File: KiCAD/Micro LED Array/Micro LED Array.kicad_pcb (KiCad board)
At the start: 2 copper layers, 36 parts

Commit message: 56 strip 2
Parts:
- added D37: LED, Custom footprints:LED_APG0603SEC-E-TT_KNB, F.Cu at (36.5, 38.5)
- added D38: LED, Custom footprints:LED_APG0603SEC-E-TT_KNB, F.Cu at (36.5, 38.9)
- added D39: LED, Custom footprints:LED_APG0603SEC-E-TT_KNB, F.Cu at (36.5, 39.4)
- added D40: LED, Custom footprints:LED_APG0603SEC-E-TT_KNB, F.Cu at (36.5, 39.9)
- added D41: LED, Custom footprints:LED_APG0603SEC-E-TT_KNB, F.Cu at (36.5, 43.8)
- added D42: LED, Custom footprints:LED_APG0603SEC-E-TT_KNB, F.Cu at (36.5, 43.3)
- added D43: LED, Custom footprints:LED_APG0603SEC-E-TT_KNB, F.Cu at (36.5, 42.8)
- added D44: LED, Custom footprints:LED_APG0603SEC-E-TT_KNB, F.Cu at (36.5, 42.3)
- added D45: LED, Custom footprints:LED_APG0603SEC-E-TT_KNB, F.Cu at (36.5, 41.9)
- added D46: LED, Custom footprints:LED_APG0603SEC-E-TT_KNB, F.Cu at (36.5, 41.4)
- added D47: LED, Custom footprints:LED_APG0603SEC-E-TT_KNB, F.Cu at (36.5, 40.9)
- added D48: LED, Custom footprints:LED_APG0603SEC-E-TT_KNB, F.Cu at (36.5, 40.4)
- added D49: LED, Custom footprints:LED_APG0603SEC-E-TT_KNB, F.Cu at (36.5, 44.3)
- added D50: LED, Custom footprints:LED_APG0603SEC-E-TT_KNB, F.Cu at (36.5, 44.8)
- added D51: LED, Custom footprints:LED_APG0603SEC-E-TT_KNB, F.Cu at (36.5, 45.2)
- added D52: LED, Custom footprints:LED_APG0603SEC-E-TT_KNB, F.Cu at (36.5, 45.7)
- added D53: LED, Custom footprints:LED_APG0603SEC-E-TT_KNB, F.Cu at (36.5, 46.2)
- added D54: LED, Custom footprints:LED_APG0603SEC-E-TT_KNB, F.Cu at (36.5, 46.7)
- added D55: LED, Custom footprints:LED_APG0603SEC-E-TT_KNB, F.Cu at (36.5, 47.2)
- added D56: LED, Custom footprints:LED_APG0603SEC-E-TT_KNB, F.Cu at (36.5, 47.7)
- D1, D10, D11, D12, D13, D14, D15, D16, D17, D18, D19, D2, D20, D21, D22, D23, D24, D25, D26, D27, D28, D29, D3, D30, D31, D32, D33, D34, D35, D36, D4, D5, D6, D7, D8, D9: footprint Custom footprints:LED_APG0603SEC-E-TT_KNB - with via -> Custom footprints:LED_APG0603SEC-E-TT_KNB
- moved D25 56.8 mm to (36.5, 36.0), turned to 180 degrees
- moved D26 55.4 mm to (36.5, 35.5)
- moved D9 55.1 mm to (36.5, 28.3), turned to 180 degrees
- moved D1 54.9 mm to (36.5, 21.0)
- moved D7 54.5 mm to (36.5, 23.9)
- moved D2 54.5 mm to (36.5, 21.5), turned to 180 degrees
- moved D19 54.3 mm to (36.5, 29.7)
- moved D10 54.1 mm to (36.5, 27.8)
- moved D27 54.1 mm to (36.5, 35.1), turned to 180 degrees
- moved D3 54.1 mm to (36.5, 22.0)
- moved D13 54.0 mm to (36.5, 26.3), turned to 180 degrees
- moved D8 54.0 mm to (36.5, 24.4), turned to 180 degrees
- moved D20 53.7 mm to (36.5, 30.2), turned to 180 degrees
- moved D4 53.7 mm to (36.5, 22.5), turned to 180 degrees
- moved D33 53.6 mm to (36.5, 36.5)
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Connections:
- D11 pad 1: Net-(D11-K) -> Net-(D10-A)
- D11 pad 2: Net-(D10-K) -> Net-(D11-A)
- D12 pad 1: Net-(D12-K) -> Net-(D11-A)
- D12 pad 2: Net-(D11-K) -> Net-(D12-A)
- D13 pad 1: Net-(D13-K) -> Net-(D12-A)
- D13 pad 2: Net-(D12-K) -> Net-(D13-A)
- D14 pad 1: Net-(D14-K) -> Net-(D13-A)
- D14 pad 2: Net-(D13-K) -> Net-(D14-A)
- D15 pad 1: Net-(D15-K) -> Net-(D14-A)
- D15 pad 2: Net-(D14-K) -> Net-(D15-A)
- D16 pad 1: Net-(D16-K) -> Net-(D15-A)
- D16 pad 2: Net-(D15-K) -> Net-(D16-A)
- D17 pad 2: Net-(D16-K) -> Net-(D17-A)
- D25 pad 2: Net-(D24-K) -> Net-(D25-A)
- D26 pad 1: Net-(D26-K) -> Net-(D25-A)
- D26 pad 2: Net-(D25-K) -> Net-(D26-A)
- D27 pad 1: Net-(D27-K) -> Net-(D26-A)
- D27 pad 2: Net-(D26-K) -> Net-(D27-A)
- D28 pad 1: Net-(D28-K) -> Net-(D27-A)
- D28 pad 2: Net-(D27-K) -> Net-(D28-A)
- D29 pad 1: Net-(D29-K) -> Net-(D28-A)
- D29 pad 2: Net-(D28-K) -> Net-(D29-A)
- D30 pad 1: Net-(D30-K) -> Net-(D29-A)
- D30 pad 2: Net-(D29-K) -> Net-(D30-A)
- D31 pad 1: Net-(D31-K) -> Net-(D30-A)
- D31 pad 2: Net-(D30-K) -> Net-(D31-A)
- D32 pad 1: Net-(D32-K) -> Net-(D31-A)
- D32 pad 2: Net-(D31-K) -> Net-(D24-K)
- D33 pad 2: Net-(D32-K) -> Net-(D25-K)
- D36 pad 1: GND -> Net-(D36-K)
- D8 pad 1: Net-(D8-K) -> Net-(D16-A)
- D9 pad 1: Net-(D10-A) -> Net-(D17-A)
- D9 pad 2: Net-(D8-K) -> Net-(D10-K)

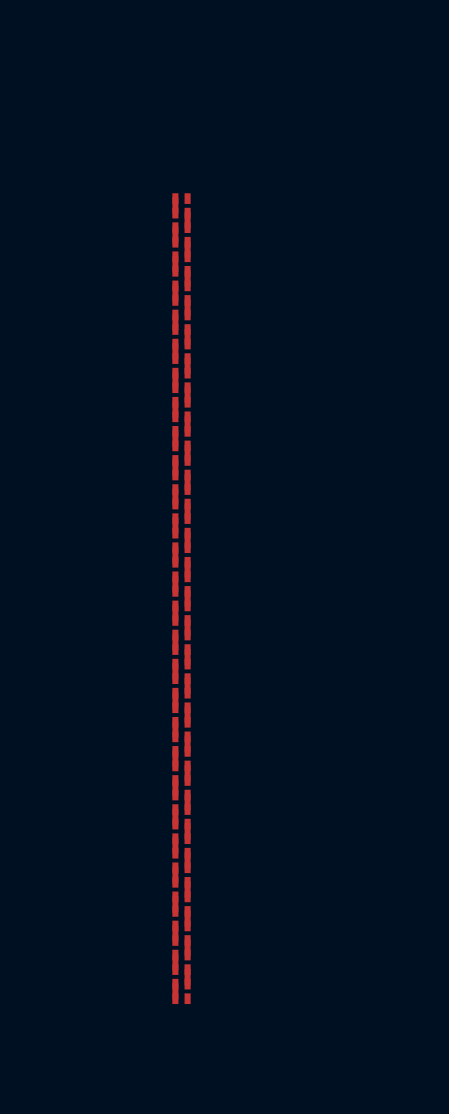
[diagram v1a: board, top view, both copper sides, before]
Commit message: Add bodge pads to diagnose and bypass LEDs
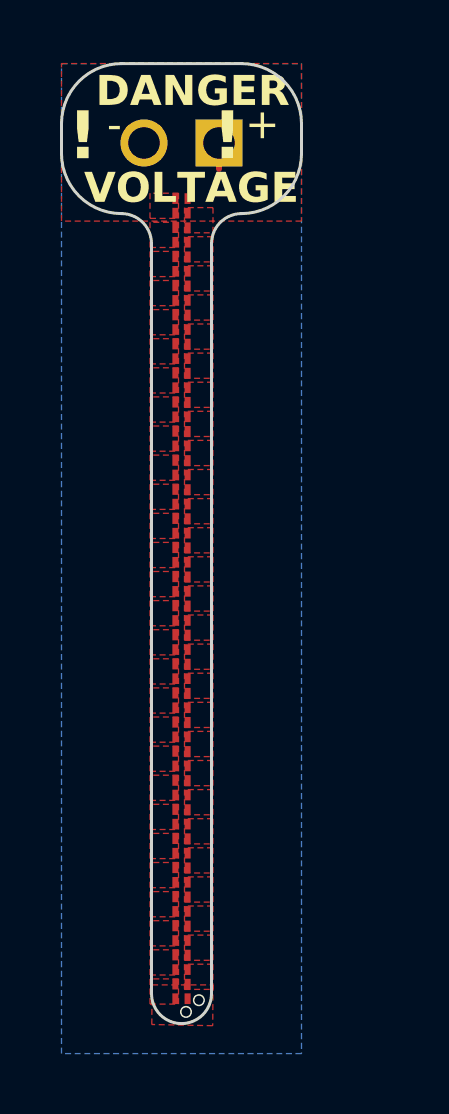
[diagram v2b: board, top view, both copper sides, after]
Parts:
- added J1: JST-XH, Custom footprints:JST_B2B-XH-A, B.Cu at (36.5, 19.7)
- turned D1 to 90 degrees
- turned D10 to 90 degrees
- turned D11 to -90 degrees
- turned D12 to 90 degrees
- turned D13 to -90 degrees
- turned D14 to 90 degrees
- turned D15 to -90 degrees
- turned D16 to 90 degrees
- turned D17 to 90 degrees
- turned D18 to -90 degrees
- turned D19 to 90 degrees
- turned D2 to -90 degrees
- turned D20 to -90 degrees
- turned D21 to 90 degrees
- turned D22 to -90 degrees
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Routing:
- net VDD: track 0.00 -> 0.87 mm
- net GND: vias 0 -> 2
- added copper zone on B.Cu, net GND
- added copper zone on F.Cu, net GND
- added copper zone on F.Cu, net Net-(D1-K)
- added copper zone on F.Cu, net Net-(D10-A)
- added copper zone on F.Cu, net Net-(D10-K)
- added copper zone on F.Cu, net Net-(D11-A)
- added copper zone on F.Cu, net Net-(D12-A)
- added copper zone on F.Cu, net Net-(D13-A)
- added copper zone on F.Cu, net Net-(D14-A)
- added copper zone on F.Cu, net Net-(D15-A)
- added copper zone on F.Cu, net Net-(D16-A)
- added copper zone on F.Cu, net Net-(D17-A)
- added copper zone on F.Cu, net Net-(D17-K)
- added copper zone on F.Cu, net Net-(D18-K)
- added copper zone on F.Cu, net Net-(D19-K)
- added copper zone on F.Cu, net Net-(D2-K)
- added copper zone on F.Cu, net Net-(D20-K)
- added copper zone on F.Cu, net Net-(D21-K)
- added copper zone on F.Cu, net Net-(D22-K)
- added copper zone on F.Cu, net Net-(D23-K)
- added copper zone on F.Cu, net Net-(D24-K)
- added copper zone on F.Cu, net Net-(D25-A)
- added copper zone on F.Cu, net Net-(D25-K)
- added copper zone on F.Cu, net Net-(D26-A)
- added copper zone on F.Cu, net Net-(D27-A)
- added copper zone on F.Cu, net Net-(D28-A)
- added copper zone on F.Cu, net Net-(D29-A)
- added copper zone on F.Cu, net Net-(D3-K)
- added copper zone on F.Cu, net Net-(D30-A)
- added copper zone on F.Cu, net Net-(D31-A)
- added copper zone on F.Cu, net Net-(D33-K)
- added copper zone on F.Cu, net Net-(D34-K)
- added copper zone on F.Cu, net Net-(D35-K)
- added copper zone on F.Cu, net Net-(D36-K)
- added copper zone on F.Cu, net Net-(D37-K)
- added copper zone on F.Cu, net Net-(D38-K)
- added copper zone on F.Cu, net Net-(D39-K)
- added copper zone on F.Cu, net Net-(D4-K)
- added copper zone on F.Cu, net Net-(D40-K)
- added copper zone on F.Cu, net Net-(D41-A)
- added copper zone on F.Cu, net Net-(D41-K)
- added copper zone on F.Cu, net Net-(D42-A)
- added copper zone on F.Cu, net Net-(D43-A)
- added copper zone on F.Cu, net Net-(D44-A)
- added copper zone on F.Cu, net Net-(D45-A)
- added copper zone on F.Cu, net Net-(D46-A)
- added copper zone on F.Cu, net Net-(D47-A)
- added copper zone on F.Cu, net Net-(D49-K)
- added copper zone on F.Cu, net Net-(D5-K)
- added copper zone on F.Cu, net Net-(D50-K)
- added copper zone on F.Cu, net Net-(D51-K)
- added copper zone on F.Cu, net Net-(D52-K)
- added copper zone on F.Cu, net Net-(D53-K)
- added copper zone on F.Cu, net Net-(D54-K)
- added copper zone on F.Cu, net Net-(D55-K)
- added copper zone on F.Cu, net Net-(D6-K)
- added copper zone on F.Cu, net Net-(D7-K)
- added copper zone on F.Cu, net VDD
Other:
- board outline added: 8 x 32 mm
- board text added: "! !"
- board text added: "+"
- board text added: "-"
- board text added: "DANGER"
- board text added: "HIGH VOLTAGE! 20 mA Max"
- board text added: "VOLTAGE"

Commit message: Current setup
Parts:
- removed D13, D14, D15, D16, D5, D6, D7, D8: LED, Custom footprints:LED_APG0603SEC-E-TT_KNB
- J1: footprint Custom footprints:JST_B2B-XH-A -> Connector_Wire:SolderWire-0.1sqmm_1x02_P3.6mm_D0.4mm_OD1mm; moved to F.Cu
- moved J1 6.10 mm to (38.3, 25.5), turned to 180 degrees
- moved D1 5.33 mm to (36.5, 26.3), turned to -90 degrees
- moved D2 4.36 mm to (36.5, 25.8), turned to 90 degrees
- moved D3 3.38 mm to (36.5, 25.4), turned to -90 degrees
- moved D4 2.41 mm to (36.5, 24.9), turned to 90 degrees
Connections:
- D1 pad 2: VDD -> Net-(D1-A)
- D12 pad 2: Net-(D12-A) -> Net-(D1-K)
- D2 pad 1: Net-(D2-K) -> Net-(D1-A)
- D2 pad 2: Net-(D1-K) -> Net-(D2-A)
- D3 pad 1: Net-(D3-K) -> Net-(D2-A)
- D3 pad 2: Net-(D2-K) -> Net-(D3-A)
- D4 pad 1: Net-(D4-K) -> Net-(D3-A)
- D4 pad 2: Net-(D3-K) -> VDD
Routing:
- net VDD: track 0.87 -> 1.95 mm
- added copper zone on F.Cu, net Net-(D1-A)
- added copper zone on F.Cu, net Net-(D2-A)
- added copper zone on F.Cu, net Net-(D3-A)
- removed copper zone on F.Cu, net Net-(D12-A)
- removed copper zone on F.Cu, net Net-(D13-A)
- removed copper zone on F.Cu, net Net-(D14-A)
- removed copper zone on F.Cu, net Net-(D15-A)
- removed copper zone on F.Cu, net Net-(D16-A)
- removed copper zone on F.Cu, net Net-(D2-K)
- removed copper zone on F.Cu, net Net-(D3-K)
- removed copper zone on F.Cu, net Net-(D4-K)
- removed copper zone on F.Cu, net Net-(D5-K)
- removed copper zone on F.Cu, net Net-(D6-K)
- removed copper zone on F.Cu, net Net-(D7-K)
- removed copper zone on F.Cu, net VDD
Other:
- board size 8 x 32 mm -> 6 x 24 mm
- board text removed: "! !"
- board text removed: "+"
- board text removed: "-"
- board text removed: "DANGER"
- board text removed: "VOLTAGE"

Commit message: Initial draft
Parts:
- removed D17, D18, D19, D20, D21, D22, D23, D24, D25, D26, D27, D28, D29, D30, D31, D32, D33, D34, D35, D36, D37, D38, D39, D40, D41, D42, D43, D44, D45, D46, D47, D48, D49, D50, D51, D52, D53, D54, D55, D56: LED, Custom footprints:LED_APG0603SEC-E-TT_KNB
- added D13: LED, Custom footprints:LED_XLAMP_XE-G_CRW, F.Cu at (31.8, 45.9)
- added D14: LED, Custom footprints:LED_XLAMP_XE-G_CRW, F.Cu at (31.8, 47.6)
- added D5: LED, Custom footprints:LED_XLAMP_XE-G_CRW, F.Cu at (31.8, 31.8)
- added D6: LED, Custom footprints:LED_XLAMP_XE-G_CRW, F.Cu at (31.8, 33.6)
- added D7: LED, Custom footprints:LED_XLAMP_XE-G_CRW, F.Cu at (31.8, 35.3)
- added D8: LED, Custom footprints:LED_XLAMP_XE-G_CRW, F.Cu at (31.8, 37.1)
- D1, D10, D11, D12, D2, D3, D4, D9: footprint Custom footprints:LED_APG0603SEC-E-TT_KNB -> Custom footprints:LED_XLAMP_XE-G_CRW
- moved D12 17.9 mm to (31.8, 44.1), turned to 180 degrees
- moved D11 15.8 mm to (31.8, 42.4), turned to 180 degrees
- moved D10 13.7 mm to (31.8, 40.6), turned to 180 degrees
- moved J1 11.7 mm to (49.3, 21.7), turned to 0 degrees
- moved D9 11.6 mm to (31.8, 38.8), turned to 180 degrees
- moved D4 7.02 mm to (31.8, 30.1), turned to 180 degrees
- moved D3 5.56 mm to (31.8, 28.3), turned to 180 degrees
- moved D1 4.95 mm to (31.8, 24.8), turned to 180 degrees
- moved D2 4.76 mm to (31.8, 26.6), turned to 180 degrees
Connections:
- D1 pad 2: Net-(D1-A) -> VDD
- D11 pad 1: Net-(D10-A) -> Net-(D11-K)
- D11 pad 2: Net-(D11-A) -> Net-(D10-K)
- D12 pad 1: Net-(D11-A) -> Net-(D12-K)
- D12 pad 2: Net-(D1-K) -> Net-(D11-K)
- D2 pad 1: Net-(D1-A) -> Net-(D2-K)
- D2 pad 2: Net-(D2-A) -> Net-(D1-K)
- D3 pad 1: Net-(D2-A) -> Net-(D3-K)
- D3 pad 2: Net-(D3-A) -> Net-(D2-K)
- D4 pad 1: Net-(D3-A) -> Net-(D4-K)
- D4 pad 2: VDD -> Net-(D3-K)
- D9 pad 1: Net-(D17-A) -> Net-(D10-A)
- D9 pad 2: Net-(D10-K) -> Net-(D8-K)
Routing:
- net VDD: track 1.95 -> 0.00 mm
- net Net-(D8-K): track 0.00 -> 0.91 mm
- net Net-(D7-K): track 0.00 -> 0.91 mm
- net Net-(D6-K): track 0.00 -> 0.91 mm
- net Net-(D5-K): track 0.00 -> 0.91 mm
- net Net-(D2-K): track 0.00 -> 0.91 mm
- net Net-(D13-K): track 0.00 -> 0.91 mm
- net Net-(D12-K): track 0.00 -> 0.91 mm
- net Net-(D11-K): track 0.00 -> 0.91 mm
- net Net-(D10-A): track 0.00 -> 0.91 mm
- net Net-(D1-K): track 0.00 -> 0.91 mm
- net Net-(D4-K): track 0.00 -> 0.91 mm
- net Net-(D3-K): track 0.00 -> 0.91 mm
- net Net-(D10-K): track 0.00 -> 0.91 mm
- added copper zone on F.Cu, net Net-(D11-K)
- added copper zone on F.Cu, net Net-(D12-K)
- added copper zone on F.Cu, net Net-(D13-K)
- added copper zone on F.Cu, net Net-(D2-K)
- added copper zone on F.Cu, net Net-(D3-K)
- added copper zone on F.Cu, net Net-(D4-K)
- added copper zone on F.Cu, net Net-(D5-K)
- added copper zone on F.Cu, net Net-(D6-K)
- added copper zone on F.Cu, net Net-(D7-K)
- added copper zone on F.Cu, net Net-(D8-K)
- removed copper zone on F.Cu, net Net-(D1-A)
- removed copper zone on F.Cu, net Net-(D11-A)
- removed copper zone on F.Cu, net Net-(D17-A)
- removed copper zone on F.Cu, net Net-(D17-K)
- removed copper zone on F.Cu, net Net-(D18-K)
- removed copper zone on F.Cu, net Net-(D19-K)
- removed copper zone on F.Cu, net Net-(D2-A)
- removed copper zone on F.Cu, net Net-(D20-K)
- removed copper zone on F.Cu, net Net-(D21-K)
- removed copper zone on F.Cu, net Net-(D22-K)
- removed copper zone on F.Cu, net Net-(D23-K)
- removed copper zone on F.Cu, net Net-(D24-K)
- removed copper zone on F.Cu, net Net-(D25-A)
- removed copper zone on F.Cu, net Net-(D25-K)
- removed copper zone on F.Cu, net Net-(D26-A)
- removed copper zone on F.Cu, net Net-(D27-A)
- removed copper zone on F.Cu, net Net-(D28-A)
- removed copper zone on F.Cu, net Net-(D29-A)
- removed copper zone on F.Cu, net Net-(D3-A)
- removed copper zone on F.Cu, net Net-(D30-A)
- removed copper zone on F.Cu, net Net-(D31-A)
- removed copper zone on F.Cu, net Net-(D33-K)
- removed copper zone on F.Cu, net Net-(D34-K)
- removed copper zone on F.Cu, net Net-(D35-K)
- removed copper zone on F.Cu, net Net-(D36-K)
- removed copper zone on F.Cu, net Net-(D37-K)
- removed copper zone on F.Cu, net Net-(D38-K)
- removed copper zone on F.Cu, net Net-(D39-K)
- removed copper zone on F.Cu, net Net-(D40-K)
- removed copper zone on F.Cu, net Net-(D41-A)
- removed copper zone on F.Cu, net Net-(D41-K)
- removed copper zone on F.Cu, net Net-(D42-A)
- removed copper zone on F.Cu, net Net-(D43-A)
- removed copper zone on F.Cu, net Net-(D44-A)
- removed copper zone on F.Cu, net Net-(D45-A)
- removed copper zone on F.Cu, net Net-(D46-A)
- removed copper zone on F.Cu, net Net-(D47-A)
- removed copper zone on F.Cu, net Net-(D49-K)
- removed copper zone on F.Cu, net Net-(D50-K)
- removed copper zone on F.Cu, net Net-(D51-K)
- removed copper zone on F.Cu, net Net-(D52-K)
- removed copper zone on F.Cu, net Net-(D53-K)
- removed copper zone on F.Cu, net Net-(D54-K)
- removed copper zone on F.Cu, net Net-(D55-K)
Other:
- board size 6 x 24 mm -> 9.5 x 24.5 mm
- board text removed: "HIGH VOLTAGE! 20 mA Max"

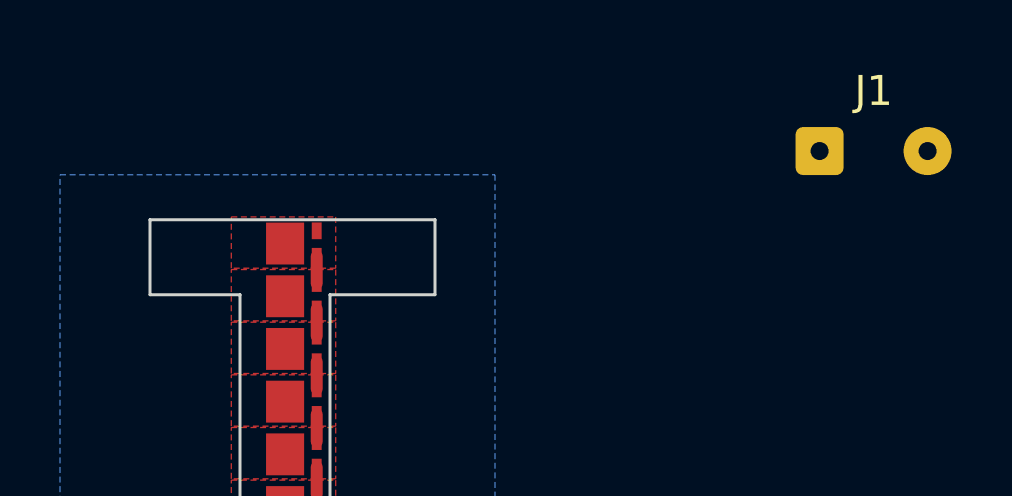
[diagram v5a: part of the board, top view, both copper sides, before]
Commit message: Widen wire spacing
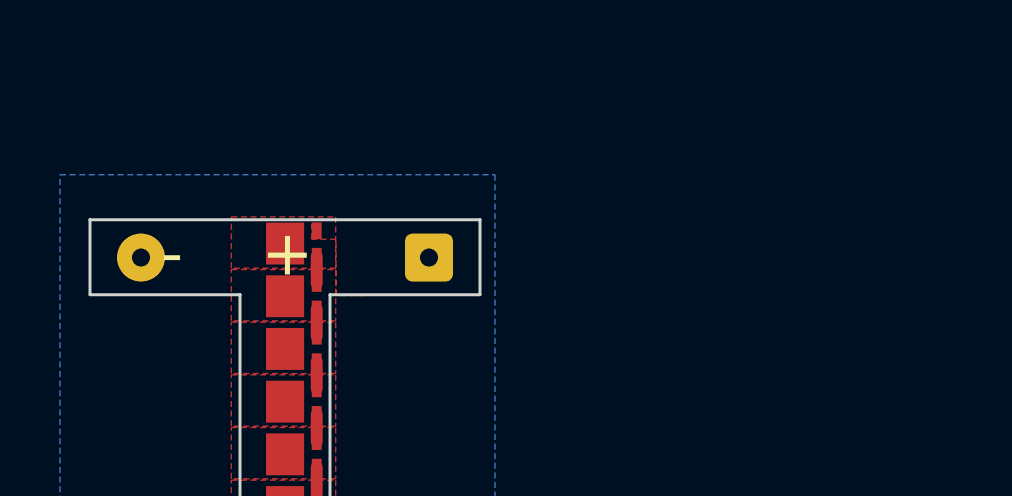
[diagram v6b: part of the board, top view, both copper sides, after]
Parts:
- J1: footprint Connector_Wire:SolderWire-0.1sqmm_1x02_P3.6mm_D0.4mm_OD1mm -> Custom footprints:SolderWire-0.1sqmm_1x02_P9.6mm_D0.4mm_OD1mm
- moved J1 13.5 mm to (36.3, 25.3), turned to 180 degrees
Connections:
- net GND renamed VSS
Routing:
- added copper zone on F.Cu, net VDD
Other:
- board size 9.5 x 24.5 mm -> 13 x 24.5 mm
- board text added: "- +"
- board text added: "DANGER"
- board text added: "HIGH VOLTAGE!"
